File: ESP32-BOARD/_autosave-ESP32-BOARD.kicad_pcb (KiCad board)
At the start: 2 copper layers, 150 x 99.9 mm, 160 parts, among them J101 Screw_Terminal_01x08, J102 Screw_Terminal_01x08, J103 Screw_Terminal_01x08, J104 Screw_Terminal_01x08, J105 Input_01x02, J106 Screw_Terminal_01x04, J120 Conn_01x07_Male, Q101 BT136-600, Q102 BT136-600, Q103 BT136-600, Q104 BT136-600, U101 LM358, U102 LM358, U103 LM2596S-ADJ, U104 LM2596S-ADJ, U105 TLP290-4, U106 TLP290-4, U107 KAQY212S, U108 KAQY212S, U109 MOC3023S, U110 MOC3023S, U111 MOC3023S, U112 MOC3023S, U113 SIM800L, U114 ESP32-dev-board

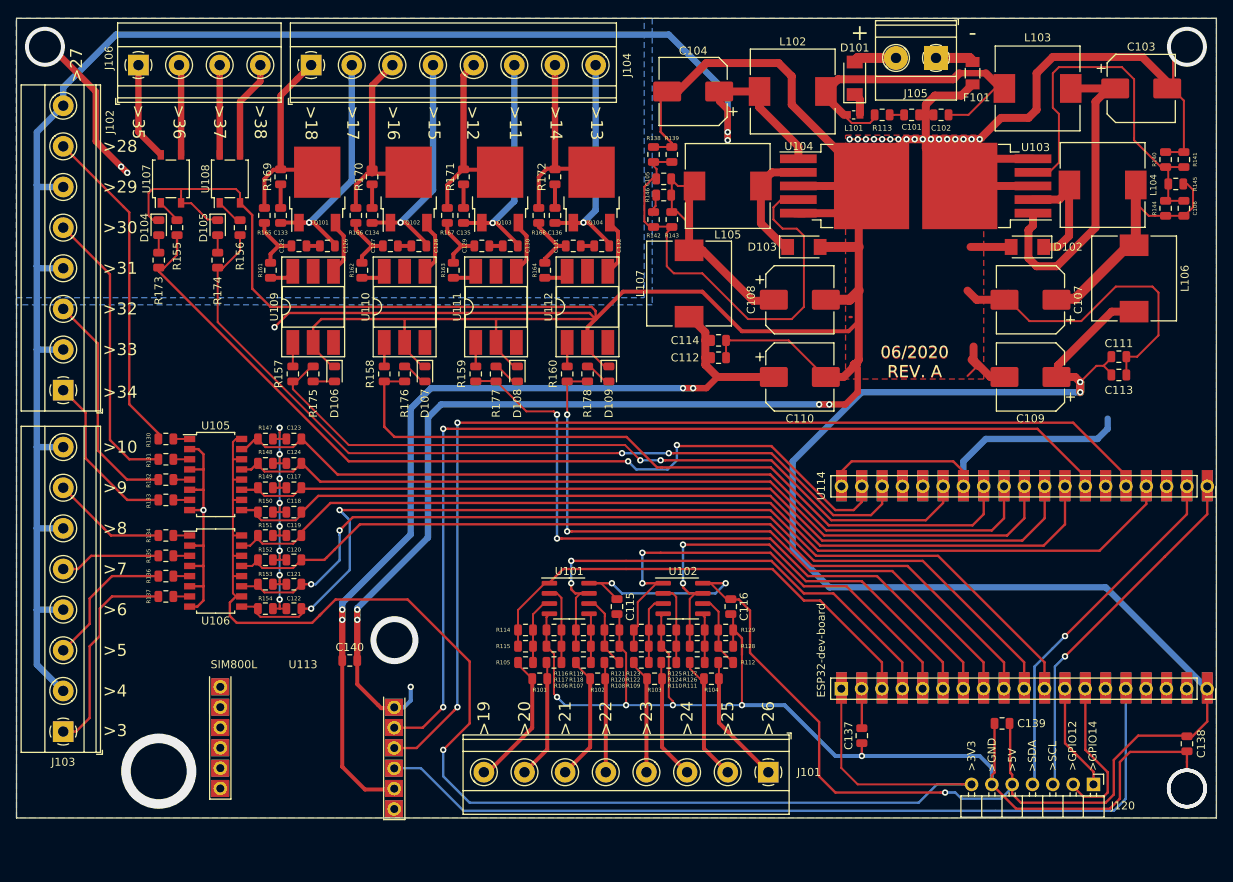
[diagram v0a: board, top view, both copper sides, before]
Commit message: arrumei as dimensoes dos furos
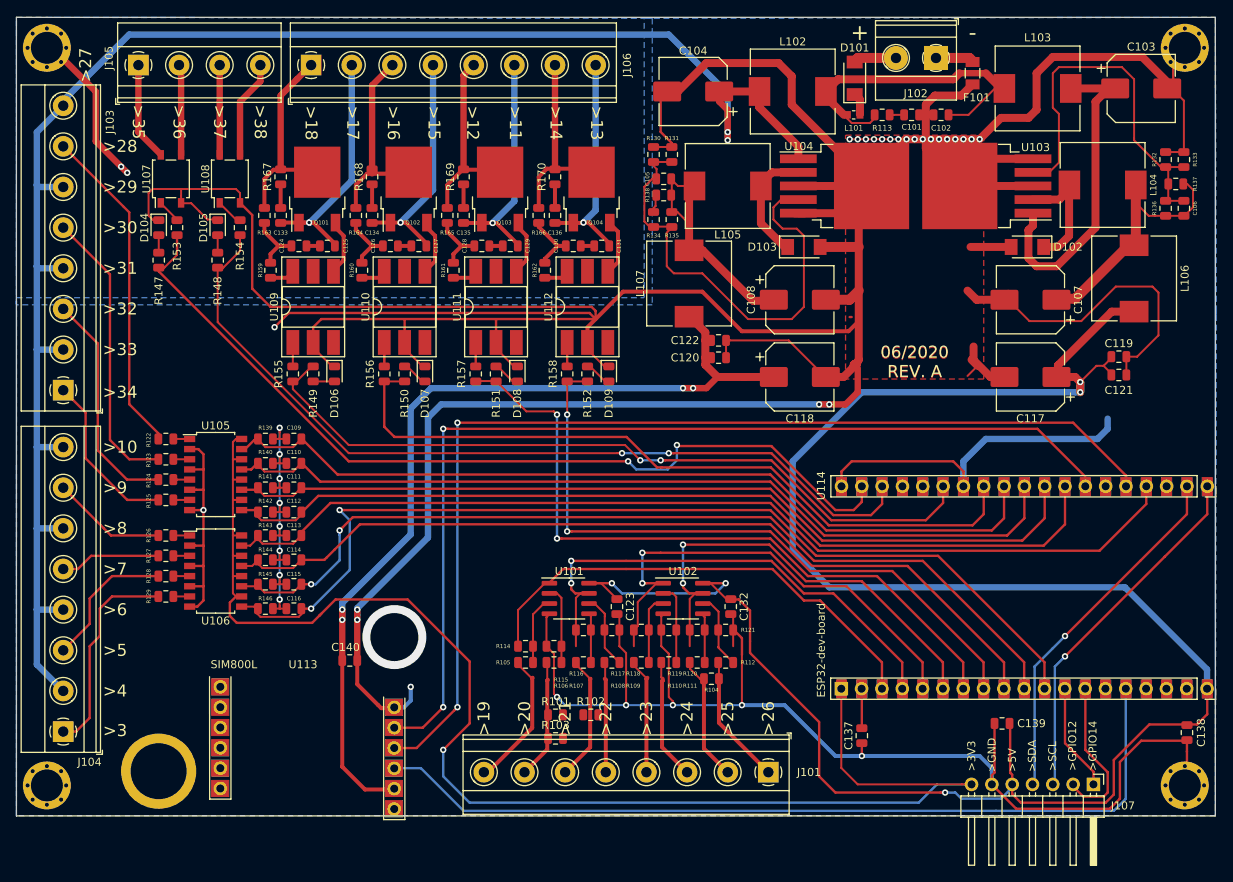
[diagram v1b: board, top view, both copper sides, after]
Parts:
- removed the R114 at (155.1, 119.6)
- removed the R116 at (158.6, 119.6)
- removed the R118 at (162.3, 121.7)
- removed the R120 at (165.9, 121.7)
- removed the R122 at (169.5, 121.7)
- removed the R124 at (173.0, 121.7)
- removed the R126 at (176.5, 121.7)
- removed the R128 at (180.1, 121.7)
- added H101: MountingHole_Pad, e-Power:MountingHole_4mm_Pad_Via, F.Cu at (95.2, 46.9)
- added H102: MountingHole_Pad, e-Power:MountingHole_4mm_Pad_Via, F.Cu at (95.2, 139.1)
- added H103: MountingHole_Pad, e-Power:MountingHole_4mm_Pad_Via, F.Cu at (237.5, 139.1)
- added H104: MountingHole_Pad, e-Power:MountingHole_4mm_Pad_Via, F.Cu at (237.5, 46.9)
- added H105: MountingHole_Pad, e-Power:MountingHole_3.2mm_M3_Pad, F.Cu at (109.2, 137.3)
- R101, R102, R103, R104: value 33R -> 15R
- U107, U108: value KAQY212S -> KAQY214S
- moved R103 14.5 mm to (158.8, 133.2)
- moved R101 4.92 mm to (158.8, 130.2)
- moved R102 4.59 mm to (163.2, 130.2)
- moved C138 1.40 mm to (237.7, 132.5)
- renumbered C123 to C109, C124 to C110, C117 to C111, C118 to C112, C119 to C113, C120 to C114, C121 to C115, C122 to C116, C109 to C117, C110 to C118, C111 to C119, C112 to C120, C113 to C121, C114 to C122, C115 to C123, C125 to C124, C126 to C125, C127 to C126, C128 to C127, C129 to C128, C130 to C129, C131 to C130, C132 to C131, C116 to C132, J105 to J102, J102 to J103, J103 to J104, J106 to J105, J104 to J106, J120 to J107, R115 to R114, R117 to R115, R119 to R116, R121 to R117, R123 to R118, R125 to R119, R127 to R120, R129 to R121, R130 to R122, R131 to R123, R132 to R124, R133 to R125, R134 to R126, R135 to R127, R136 to R128, R137 to R129, R138 to R130, R139 to R131, R140 to R132, R141 to R133, R142 to R134, R143 to R135, R144 to R136, R145 to R137, R146 to R138, R147 to R139, R148 to R140, R149 to R141, R150 to R142, R151 to R143, R152 to R144, R153 to R145, R154 to R146, R173 to R147, R174 to R148, R175 to R149, R176 to R150, R177 to R151, R178 to R152, R155 to R153, R156 to R154, R157 to R155, R158 to R156, R159 to R157, R160 to R158, R161 to R159, R162 to R160, R163 to R161, R164 to R162, R165 to R163, R166 to R164, R167 to R165, R168 to R166, R169 to R167, R170 to R168, R171 to R169, R172 to R170
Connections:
- U101 pad 2: Net-(R106-Pad1) -> Net-(R105-Pad1)
- U101 pad 3: Net-(R105-Pad1) -> Net-(R106-Pad1)
- U101 pad 5: Net-(R107-Pad1) -> Net-(R108-Pad1)
- U101 pad 6: Net-(R108-Pad1) -> Net-(R107-Pad1)
- U102 pad 2: Net-(R110-Pad1) -> Net-(R109-Pad1)
- U102 pad 3: Net-(R109-Pad1) -> Net-(R110-Pad1)
- U102 pad 5: Net-(R111-Pad1) -> Net-(R112-Pad1)
- U102 pad 6: Net-(R112-Pad1) -> Net-(R111-Pad1)
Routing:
- net GND: track 884.2 -> 906.7 mm, vias 41 -> 39
- net (no net): track 20.5 -> 0.00 mm, vias 4 -> 1
- net +5V: track 263.5 -> 264.6 mm
- net VCC: track 214.8 -> 213.8 mm
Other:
- board size 150 x 99.9 mm -> 149.9 x 99.8 mm
